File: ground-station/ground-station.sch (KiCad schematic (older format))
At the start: 43 parts, among them J1 Conn_01x02, J10 Conn_01x02, J2 Conn_01x02, J3 Conn_01x02, J4 Conn_01x02, J5 Conn_01x05, J6 Conn_01x04, J7 USB_B_Micro, J8 Conn_01x02, J9 Conn_01x02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

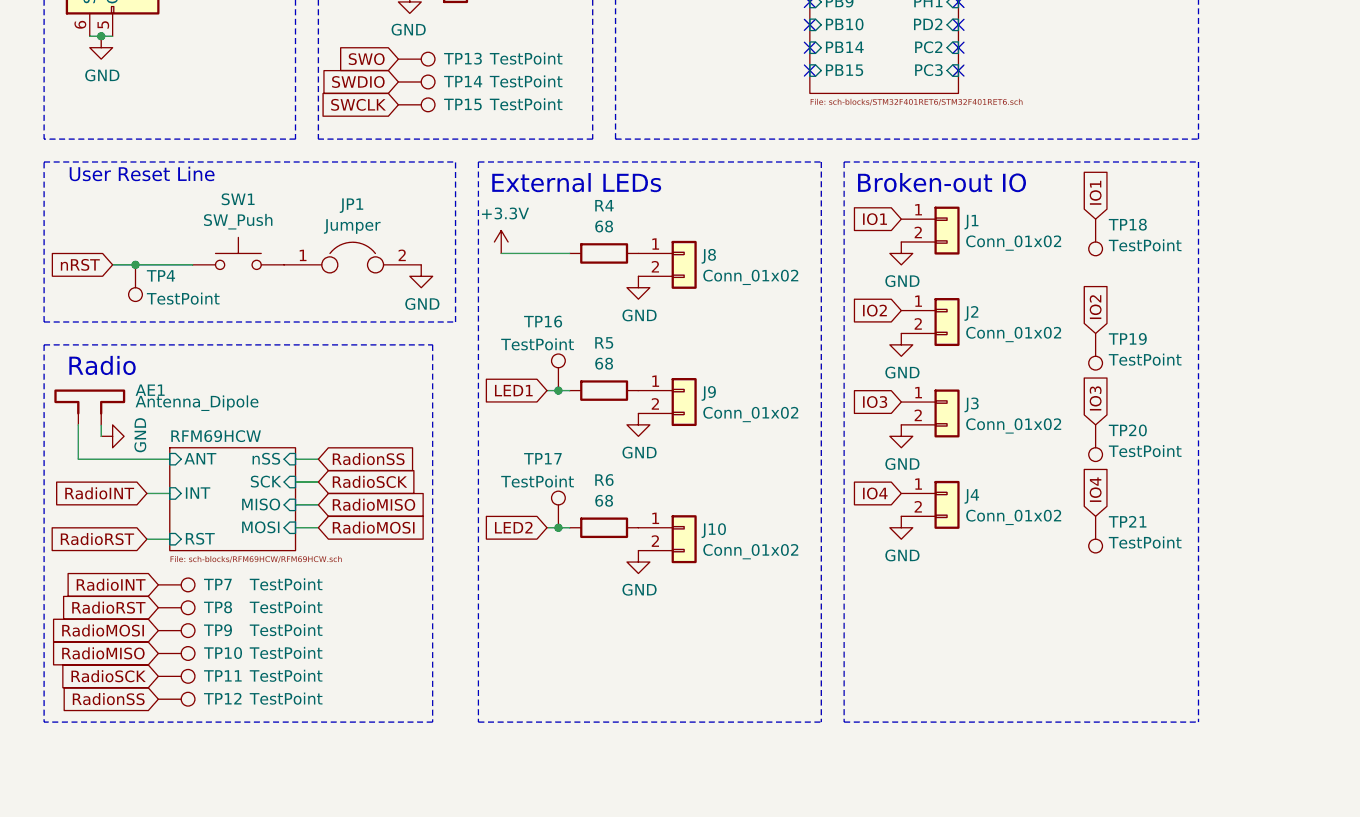
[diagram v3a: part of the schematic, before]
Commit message: mounting holes, more uniform connectors
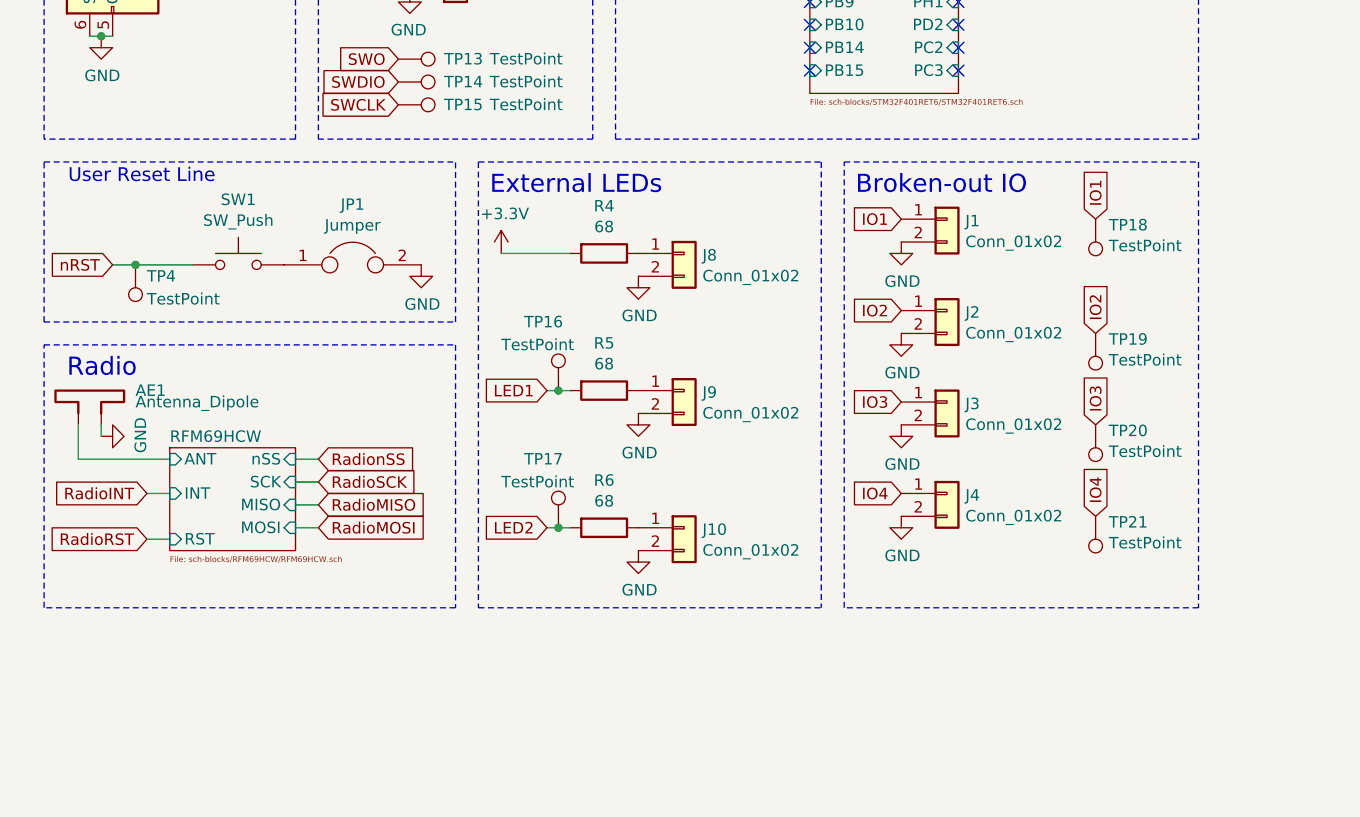
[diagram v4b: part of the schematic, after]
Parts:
- removed TP10, TP11, TP12, TP7, TP8, TP9: TestPoint, TestPoint:TestPoint_THTPad_D1.0mm_Drill0.5mm, symbol Connector:TestPoint
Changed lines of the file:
@@
 EESchema Schematic File Version 4
-LIBS:ground-station-cache
 EELAYER 30 0
 EELAYER END
@@
 Text Notes 2500 4400 0    79   ~ 0
 External LEDs
-Wire Notes Line
-	2450 4250 3950 4250
 $Comp
 L Connector_Generic:Conn_01x02 J1
@@
 	1    0    0    -1
 $EndComp
-Wire Notes Line
-	550  5050 2250 5050
 $Comp
 L Connector_Generic:Conn_01x04 J6
@@
 	0    1    1    0
 $EndComp
-Text GLabel 1050 6100 0    50   Input ~ 0
-RadioINT
-Text GLabel 1050 6200 0    50   Input ~ 0
-RadioRST
-Text GLabel 1050 6600 0    50   Input ~ 0
-RadionSS
-Text GLabel 1050 6500 0    50   Input ~ 0
-RadioSCK
-Text GLabel 1050 6400 0    50   Input ~ 0
-RadioMISO
-Text GLabel 1050 6300 0    50   Input ~ 0
-RadioMOSI
-$Comp
-L Connector:TestPoint TP7
-U 1 1 5DEB532E
-P 1050 6100
-F 0 "TP7" V 1050 6300 50  0000 L CNN
-F 1 "TestPoint" V 1050 6500 50  0000 L CNN
-F 2 "TestPoint:TestPoint_THTPad_D1.0mm_Drill0.5mm" H 1250 6100 50  0001 C CNN
-F 3 "~" H 1250 6100 50  0001 C CNN
-	1    1050 6100
-	0    1    1    0
-$EndComp
-$Comp
-L Connector:TestPoint TP8
-U 1 1 5DEB5925
-P 1050 6200
-F 0 "TP8" V 1050 6400 50  0000 L CNN
-F 1 "TestPoint" V 1050 6600 50  0000 L CNN
-F 2 "TestPoint:TestPoint_THTPad_D1.0mm_Drill0.5mm" H 1250 6200 50  0001 C CNN
-F 3 "~" H 1250 6200 50  0001 C CNN
-	1    1050 6200
-	0    1    1    0
-$EndComp
-$Comp
-L Connector:TestPoint TP9
-U 1 1 5DEB5BC5
-P 1050 6300
-F 0 "TP9" V 1050 6500 50  0000 L CNN
-F 1 "TestPoint" V 1050 6700 50  0000 L CNN
-F 2 "TestPoint:TestPoint_THTPad_D1.0mm_Drill0.5mm" H 1250 6300 50  0001 C CNN
-F 3 "~" H 1250 6300 50  0001 C CNN
-	1    1050 6300
-	0    1    1    0
-$EndComp
-$Comp
-L Connector:TestPoint TP10
-U 1 1 5DEB5CC9
-P 1050 6400
-F 0 "TP10" V 1050 6600 50  0000 L CNN
-F 1 "TestPoint" V 1050 6800 50  0000 L CNN
-F 2 "TestPoint:TestPoint_THTPad_D1.0mm_Drill0.5mm" H 1250 6400 50  0001 C CNN
-F 3 "~" H 1250 6400 50  0001 C CNN
-	1    1050 6400
-	0    1    1    0
-$EndComp
-$Comp
-L Connector:TestPoint TP11
-U 1 1 5DEB5DED
-P 1050 6500
-F 0 "TP11" V 1050 6700 50  0000 L CNN
-F 1 "TestPoint" V 1050 6900 50  0000 L CNN
-F 2 "TestPoint:TestPoint_THTPad_D1.0mm_Drill0.5mm" H 1250 6500 50  0001 C CNN
-F 3 "~" H 1250 6500 50  0001 C CNN
-	1    1050 6500
-	0    1    1    0
-$EndComp
-$Comp
-L Connector:TestPoint TP12
-U 1 1 5DEB5FA3
-P 1050 6600
-F 0 "TP12" V 1050 6800 50  0000 L CNN
-F 1 "TestPoint" V 1050 7000 50  0000 L CNN
-F 2 "TestPoint:TestPoint_THTPad_D1.0mm_Drill0.5mm" H 1250 6600 50  0001 C CNN
-F 3 "~" H 1250 6600 50  0001 C CNN
-	1    1050 6600
-	0    1    1    0
-$EndComp
-Wire Notes Line
-	2250 6700 550  6700
-Wire Notes Line
-	2250 5050 2250 6700
-Wire Notes Line
-	550  5050 550  6700
 Text GLabel 5150 4500 1    50   Input ~ 0
 IO1
@@
 Wire Notes Line
 	1900 1700 1900 2600
-Wire Notes Line
-	2450 6700 3950 6700
-Wire Notes Line
-	3950 4250 3950 6700
-Wire Notes Line
-	2450 4250 2450 6700
-Wire Notes Line
-	4050 6700 5600 6700
-Wire Notes Line
-	4050 4250 4050 6700
-Wire Notes Line
-	5600 4250 5600 6700
 Wire Notes Line
 	5600 4150 5600 550
@@
 Wire Wire Line
 	1000 5900 1100 5900
+Wire Notes Line
+	2350 5050 2350 6200
+Wire Notes Line
+	2350 6200 550  6200
+Wire Notes Line
+	550  6200 550  5050
+Wire Notes Line
+	550  5050 2350 5050
+Wire Notes Line
+	2450 6200 3950 6200
+Wire Notes Line
+	2450 4250 2450 6200
+Wire Notes Line
+	3950 4250 3950 6200
+Wire Notes Line
+	2450 4250 3950 4250
+Wire Notes Line
+	5600 4250 5600 6200
+Wire Notes Line
+	5600 6200 4050 6200
+Wire Notes Line
+	4050 6200 4050 4250
 $EndSCHEMATC

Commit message: changes from first review from aled and rajiv
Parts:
- C2: value 33uF -> 47uF
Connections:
- no-connect marks 31 -> 32
